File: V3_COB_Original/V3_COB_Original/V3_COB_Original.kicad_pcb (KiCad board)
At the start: 4 copper layers, 14 x 16 mm, 5 parts, among them J101 Conn_02x35_Counter_Clockwise_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

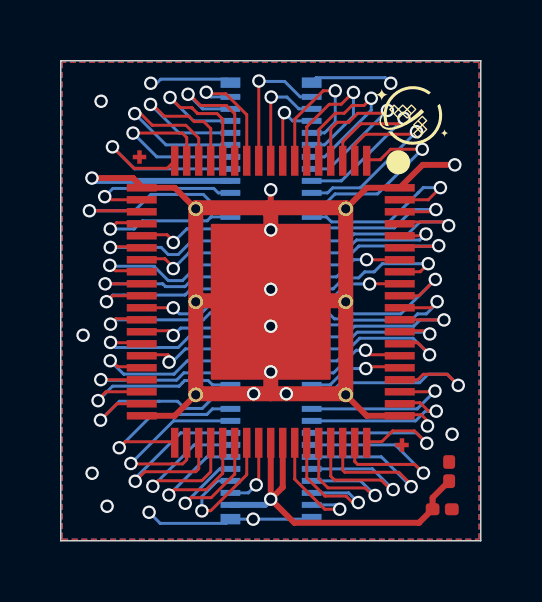
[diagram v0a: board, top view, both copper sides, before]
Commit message: xp re-route the wire for original design to make chip in correct direction
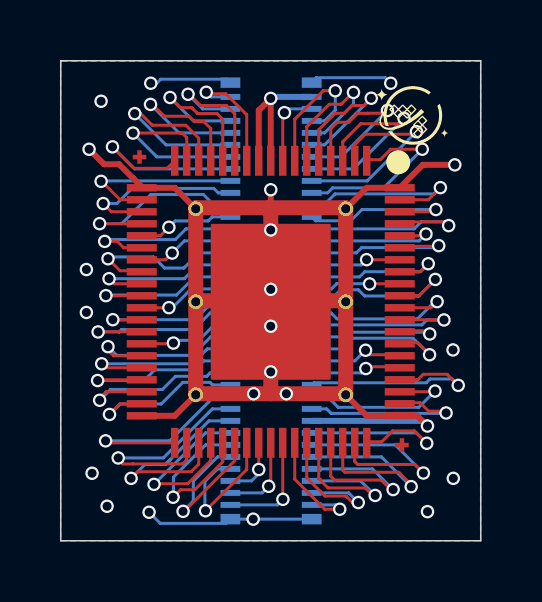
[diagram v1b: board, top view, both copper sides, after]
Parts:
- removed C102, C108: C_Small, Capacitor_SMD:C_0201_0603Metric
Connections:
- J101 pad 1: /PIN 67 -> VDD
- J101 pad 10: /PIN 58 -> /PIN 19
- J101 pad 11: /PIN 56 -> /PIN 18
- J101 pad 12: /PIN 55 -> /PIN 17
- J101 pad 13: /PIN 54 -> /PIN 16
- J101 pad 14: /PIN 53 -> /PIN 15
- J101 pad 15: /PIN 52 -> /PIN 14
- J101 pad 16: /PIN 51 -> /PIN 13
- J101 pad 17: /PIN 50 -> /PIN 12
- J101 pad 18: /PIN 49 -> /PIN 11
- J101 pad 19: /PIN 48 -> /PIN 10
- J101 pad 2: /PIN 66 -> /PIN 28
- J101 pad 20: /PIN 47 -> /PIN 9
- J101 pad 21: /PIN 46 -> /PIN 8
- J101 pad 22: /PIN 45 -> /PIN 7
- J101 pad 23: /PIN 44 -> /PIN 6
- J101 pad 24: /PIN 43 -> /PIN 5
- J101 pad 25: /PIN 42 -> /PIN 4
- J101 pad 26: /PIN 41 -> /PIN 3
- J101 pad 27: /PIN 40 -> /PIN 2
- J101 pad 28: /PIN 39 -> GND
- J101 pad 29: /PIN 37 -> /PIN 74
- J101 pad 3: /PIN 65 -> /PIN 27
- J101 pad 30: /PIN 36 -> /PIN 73
- J101 pad 31: /PIN 35 -> /PIN 72
- J101 pad 32: /PIN 34 -> /PIN 71
- J101 pad 33: /PIN 33 -> /PIN 70
- J101 pad 34: /PIN 32 -> /PIN 69
- J101 pad 35: /PIN 31 -> /PIN 68
- J101 pad 36: VDD -> /PIN 67
- J101 pad 37: /PIN 28 -> /PIN 66
- J101 pad 38: /PIN 27 -> /PIN 65
- J101 pad 39: /PIN 26 -> /PIN 64
- J101 pad 4: /PIN 64 -> /PIN 26
- J101 pad 40: /PIN 25 -> /PIN 63
- J101 pad 41: /PIN 24 -> /PIN 62
- J101 pad 42: /PIN 23 -> /PIN 61
- J101 pad 43: /PIN 22 -> /PIN 60
- J101 pad 44: /PIN 21 -> /PIN 59
- J101 pad 45: /PIN 19 -> /PIN 58
- J101 pad 46: /PIN 18 -> /PIN 56
- J101 pad 47: /PIN 17 -> /PIN 55
- J101 pad 48: /PIN 16 -> /PIN 54
- J101 pad 49: /PIN 15 -> /PIN 53
- J101 pad 5: /PIN 63 -> /PIN 25
- J101 pad 50: /PIN 14 -> /PIN 52
- J101 pad 51: /PIN 13 -> /PIN 51
- J101 pad 52: /PIN 12 -> /PIN 50
- J101 pad 53: /PIN 11 -> /PIN 49
- J101 pad 54: /PIN 10 -> /PIN 48
- J101 pad 55: /PIN 9 -> /PIN 47
- J101 pad 56: /PIN 8 -> /PIN 46
- J101 pad 57: /PIN 7 -> /PIN 45
- J101 pad 58: /PIN 6 -> /PIN 44
- J101 pad 59: /PIN 5 -> /PIN 43
- J101 pad 6: /PIN 62 -> /PIN 24
- J101 pad 60: /PIN 4 -> /PIN 42
- J101 pad 61: /PIN 3 -> /PIN 41
- J101 pad 62: /PIN 2 -> /PIN 40
- J101 pad 63: GND -> /PIN 39
- J101 pad 64: /PIN 74 -> /PIN 37
- J101 pad 65: /PIN 73 -> /PIN 36
- J101 pad 66: /PIN 72 -> /PIN 35
- J101 pad 67: /PIN 71 -> /PIN 34
- J101 pad 68: /PIN 70 -> /PIN 33
- J101 pad 69: /PIN 69 -> /PIN 32
- J101 pad 7: /PIN 61 -> /PIN 23
- J101 pad 70: /PIN 68 -> /PIN 31
- J101 pad 8: /PIN 60 -> /PIN 22
- J101 pad 9: /PIN 59 -> /PIN 21
- U102 pad 10: /PIN 10 -> /PIN 47
- U102 pad 11: /PIN 11 -> /PIN 48
- U102 pad 12: /PIN 12 -> /PIN 49
- U102 pad 13: /PIN 13 -> /PIN 50
- U102 pad 14: /PIN 14 -> /PIN 51
- U102 pad 15: /PIN 15 -> /PIN 52
- U102 pad 16: /PIN 16 -> /PIN 53
- U102 pad 17: /PIN 17 -> /PIN 54
- U102 pad 18: /PIN 18 -> /PIN 55
- U102 pad 19: /PIN 19 -> /PIN 56
- U102 pad 2: /PIN 2 -> /PIN 39
- U102 pad 21: /PIN 21 -> /PIN 58
- U102 pad 22: /PIN 22 -> /PIN 59
- U102 pad 23: /PIN 23 -> /PIN 60
- U102 pad 24: /PIN 24 -> /PIN 61
- U102 pad 25: /PIN 25 -> /PIN 62
- U102 pad 26: /PIN 26 -> /PIN 63
- U102 pad 27: /PIN 27 -> /PIN 64
- U102 pad 28: /PIN 28 -> /PIN 65
- U102 pad 29: VDD -> /PIN 66
- U102 pad 3: /PIN 3 -> /PIN 40
- U102 pad 30: VDD -> /PIN 67
- U102 pad 31: /PIN 31 -> /PIN 68
- U102 pad 32: /PIN 32 -> /PIN 69
- U102 pad 33: /PIN 33 -> /PIN 70
- U102 pad 34: /PIN 34 -> /PIN 71
- U102 pad 35: /PIN 35 -> /PIN 72
- U102 pad 36: /PIN 36 -> /PIN 73
- U102 pad 37: /PIN 37 -> /PIN 74
- U102 pad 39: /PIN 39 -> /PIN 2
- U102 pad 4: /PIN 4 -> /PIN 41
- U102 pad 40: /PIN 40 -> /PIN 3
- U102 pad 41: /PIN 41 -> /PIN 4
- U102 pad 42: /PIN 42 -> /PIN 5
- U102 pad 43: /PIN 43 -> /PIN 6
- U102 pad 44: /PIN 44 -> /PIN 7
- U102 pad 45: /PIN 45 -> /PIN 8
- U102 pad 46: /PIN 46 -> /PIN 9
- U102 pad 47: /PIN 47 -> /PIN 10
- U102 pad 48: /PIN 48 -> /PIN 11
- U102 pad 49: /PIN 49 -> /PIN 12
- U102 pad 5: /PIN 5 -> /PIN 42
- U102 pad 50: /PIN 50 -> /PIN 13
- U102 pad 51: /PIN 51 -> /PIN 14
- U102 pad 52: /PIN 52 -> /PIN 15
- U102 pad 53: /PIN 53 -> /PIN 16
- U102 pad 54: /PIN 54 -> /PIN 17
- U102 pad 55: /PIN 55 -> /PIN 18
- U102 pad 56: /PIN 56 -> /PIN 19
- U102 pad 58: /PIN 58 -> /PIN 21
- U102 pad 59: /PIN 59 -> /PIN 22
- U102 pad 6: /PIN 6 -> /PIN 43
- U102 pad 60: /PIN 60 -> /PIN 23
- U102 pad 61: /PIN 61 -> /PIN 24
- U102 pad 62: /PIN 62 -> /PIN 25
- U102 pad 63: /PIN 63 -> /PIN 26
- U102 pad 64: /PIN 64 -> /PIN 27
- U102 pad 65: /PIN 65 -> /PIN 28
- U102 pad 66: /PIN 66 -> VDD
- U102 pad 67: /PIN 67 -> VDD
- U102 pad 68: /PIN 68 -> /PIN 31
- U102 pad 69: /PIN 69 -> /PIN 32
- U102 pad 7: /PIN 7 -> /PIN 44
- U102 pad 70: /PIN 70 -> /PIN 33
- U102 pad 71: /PIN 71 -> /PIN 34
- U102 pad 72: /PIN 72 -> /PIN 35
- U102 pad 73: /PIN 73 -> /PIN 36
- U102 pad 74: /PIN 74 -> /PIN 37
- U102 pad 8: /PIN 8 -> /PIN 45
- U102 pad 9: /PIN 9 -> /PIN 46
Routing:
- net VDD: track 12.4 -> 5.80 mm
- net /PIN 48: track 6.16 -> 3.27 mm
- net /PIN 11: track 3.33 -> 6.00 mm
- net /PIN 44: track 5.87 -> 3.22 mm
- net /PIN 12: track 5.40 -> 2.99 mm
- net /PIN 7: track 3.34 -> 5.72 mm
- net /PIN 15: track 3.42 -> 5.80 mm
- net /PIN 14: track 5.38 -> 3.12 mm
- net /PIN 43: track 3.47 -> 5.70 mm
- net /PIN 6: track 5.35 -> 3.16 mm
- net /PIN 49: track 3.17 -> 5.14 mm
- net /PIN 13: track 3.17 -> 5.13 mm
- net /PIN 4: track 5.35 -> 7.23 mm
- net /PIN 41: track 7.53 -> 6.31 mm
- net /PIN 3: track 6.81 -> 5.63 mm
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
